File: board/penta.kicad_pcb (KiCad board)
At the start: 2 copper layers, 37.4 x 37.4 mm, 130 parts

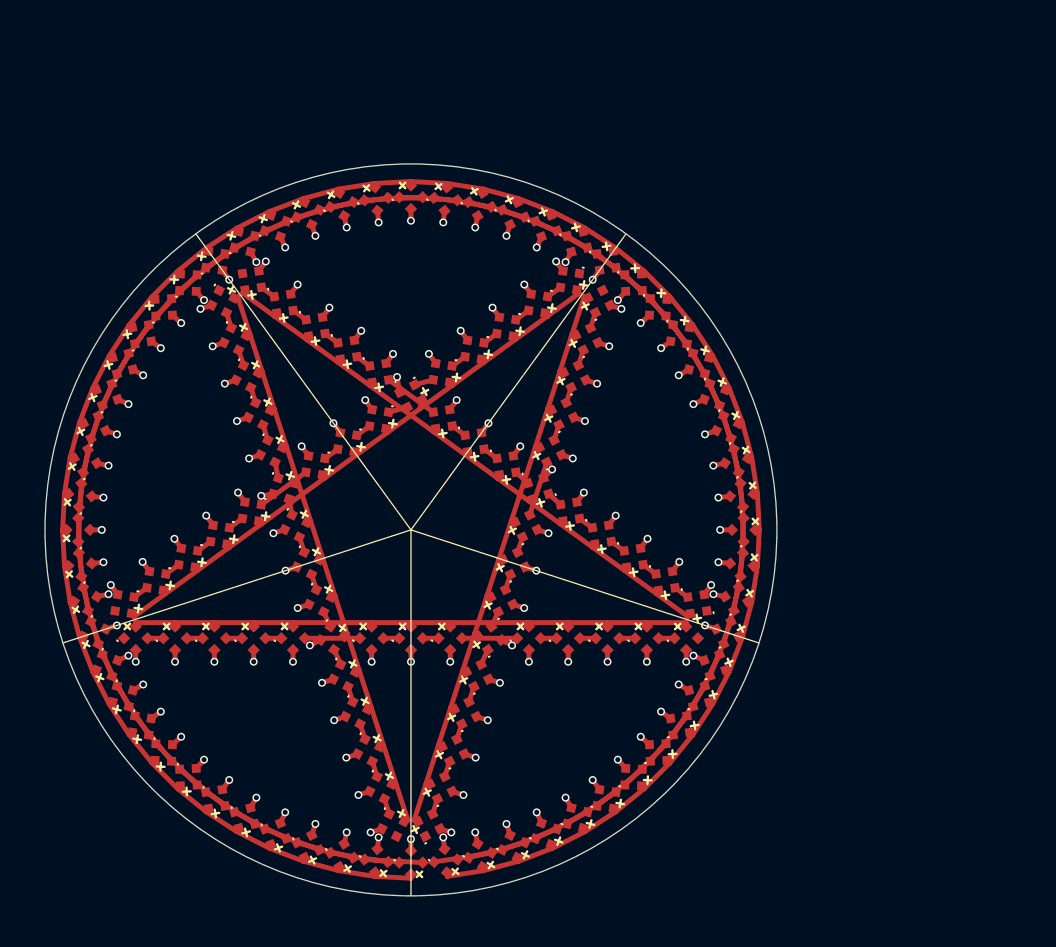
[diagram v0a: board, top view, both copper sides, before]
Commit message: candidate pixel layout + RP2040 + microphone + USB
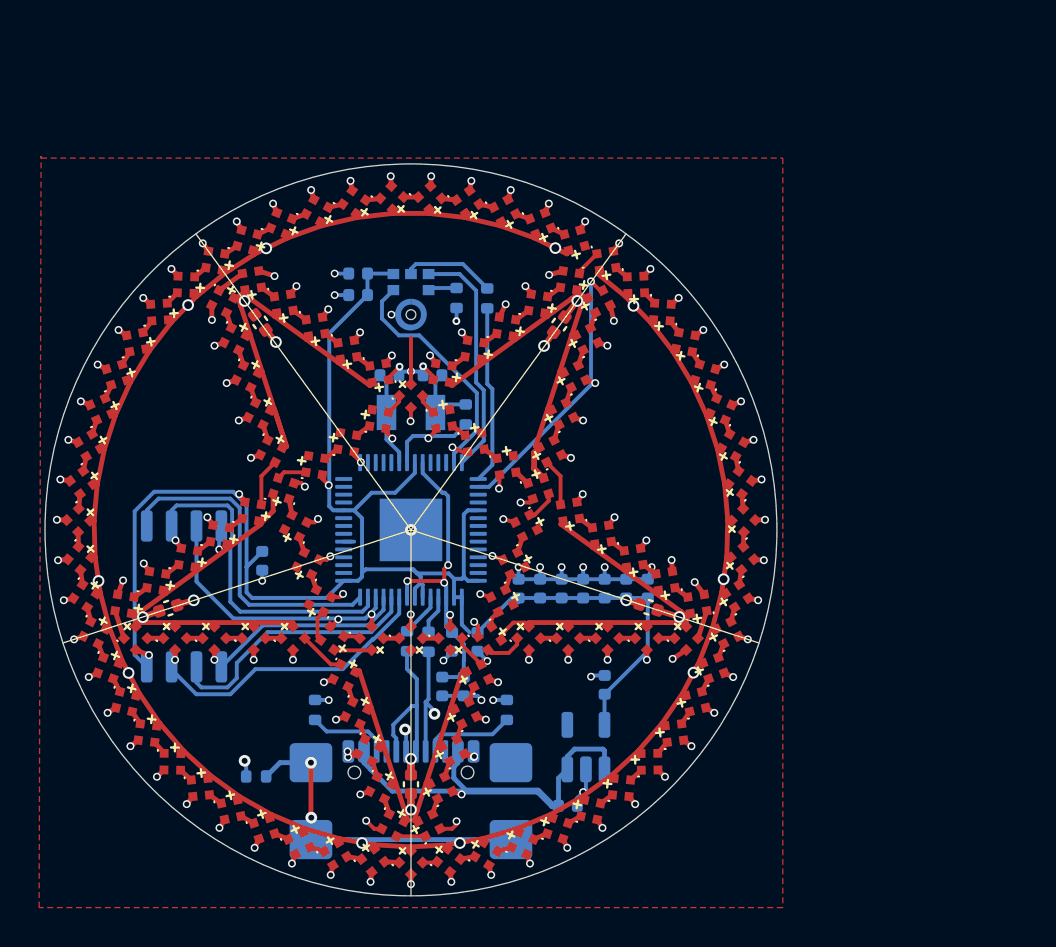
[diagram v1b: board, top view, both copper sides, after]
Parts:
- removed D126, D127, D128, D129, D130: XL-1010RGBC-WS2812B, ws2812b_1010
- added C10: 100n, Capacitor_SMD:C_0402_1005Metric, B.Cu at (106.6, 103.0)
- added C11: 100n, Capacitor_SMD:C_0402_1005Metric, B.Cu at (107.7, 103.0)
- added C12: 100n, Capacitor_SMD:C_0402_1005Metric, B.Cu at (108.8, 103.0)
- added C13: 100n, Capacitor_SMD:C_0402_1005Metric, B.Cu at (109.9, 103.0)
- added C14: 100n, Capacitor_SMD:C_0402_1005Metric, B.Cu at (111.0, 103.0)
- added C15: 100n, Capacitor_SMD:C_0402_1005Metric, B.Cu at (112.1, 103.0)
- added C16: 1u, Capacitor_SMD:C_0402_1005Metric, B.Cu at (102.1, 105.7)
- added C17: 100n, Capacitor_SMD:C_0402_1005Metric, B.Cu at (102.7, 108.0)
- added C18: 100n, Capacitor_SMD:C_0402_1005Metric, B.Cu at (101.6, 108.0)
- added C19: 100n, Capacitor_SMD:C_0402_1005Metric, B.Cu at (92.4, 101.6)
- added C2: 1uF, Capacitor_SMD:C_0402_1005Metric, B.Cu at (108.0, 114.1)
- added C20: 10u, Capacitor_SMD:C_0402_1005Metric, F.Cu at (100.0, 113.0)
- added C21: 10u, Capacitor_SMD:C_0402_1005Metric, F.Cu at (112.1, 104.0)
- added C22: 10u, Capacitor_SMD:C_0402_1005Metric, F.Cu at (107.6, 89.5)
- added C23: 10u, Capacitor_SMD:C_0402_1005Metric, F.Cu at (92.3, 89.4)
- added C24: 10u, Capacitor_SMD:C_0402_1005Metric, F.Cu at (87.6, 104.0)
- added C3: 1uF, Capacitor_SMD:C_0402_1005Metric, B.Cu at (109.9, 107.9)
- added C4: 220pF, Capacitor_SMD:C_0402_1005Metric, B.Cu at (97.3, 86.9)
- added C5: 1uF, Capacitor_SMD:C_0402_1005Metric, B.Cu at (97.3, 88.0)
- added C6: 27pF, Capacitor_SMD:C_0402_1005Metric, B.Cu at (98.9, 92.1)
- added C7: 27pF, Capacitor_SMD:C_0402_1005Metric, B.Cu at (101.1, 92.1)
- added C8: 1u, Capacitor_SMD:C_0402_1005Metric, B.Cu at (103.4, 105.7)
- added C9: 100n, Capacitor_SMD:C_0402_1005Metric, B.Cu at (105.5, 103.0)
- added J1: USB_C_Receptacle, Connector_USB:USB_C_Receptacle_GCT_USB4110, B.Cu at (100.0, 115.0)
- added MK1: SPH0645LM4H-B, penta:MIC_SPH0645LM4H-B, B.Cu at (100.0, 89.0)
- added R1: 5.11K, Resistor_SMD:R_0402_1005Metric, B.Cu at (104.9, 109.2)
- added R2: 5.11K, Resistor_SMD:R_0402_1005Metric, B.Cu at (95.1, 109.2)
- added R3: 1M, Resistor_SMD:R_0402_1005Metric, B.Cu at (92.1, 112.6)
- added R4: 68, Resistor_SMD:R_0402_1005Metric, B.Cu at (103.9, 88.2)
- added R5: 10K, Resistor_SMD:R_0402_1005Metric, B.Cu at (102.3, 88.2)
- added R6: 1k, Resistor_SMD:R_0402_1005Metric, B.Cu at (102.8, 94.1)
- added R7: 27, Resistor_SMD:R_0402_1005Metric, B.Cu at (100.9, 105.7)
- added R8: 27, Resistor_SMD:R_0402_1005Metric, B.Cu at (99.8, 105.7)
- added U1: MIC5504-3.3YM5, Package_TO_SOT_SMD:SOT-23-5, B.Cu at (108.9, 111.1)
- added U2: RP2040, Package_DFN_QFN:QFN-56-1EP_7x7mm_P0.4mm_EP3.2x3.2mm, B.Cu at (100.0, 100.0)
- added U3: W25Q32JVSS, Package_SO:SOIC-8_5.23x5.23mm_P1.27mm, B.Cu at (88.4, 103.4)
- added Y1: 12000Hz, Crystal:Crystal_SMD_3215-2Pin_3.2x1.5mm, B.Cu at (100.0, 94.0)
- D1, D10, D100, D101, D102, D103, D104, D105, D106, D107, D108, D109, D11, D110, D111, D112, D113, D114, D115, D116, D117, D118, D119, D12, D120, D121, D122, D123, D124, D125, D13, D14, D15, D16, D17, D18, D19, D2, D20, D21, D22, D23, D24, D25, D26, D27, D28, D29, D3, D30, D31, D32, D33, D34, D35, D36, D37, D38, D39, D4, D40, D41, D42, D43, D44, D45, D46, D47, D48, D49, D5, D50, D51, D52, D53, D54, D55, D56, D57, D58, D59, D6, D60, D61, D62, D63, D64, D65, D66, D67, D68, D69, D7, D70, D71, D72, D73, D74, D75, D76, D77, D78, D79, D8, D80, D81, D82, D83, D84, D85, D86, D87, D88, D89, D9, D90, D91, D92, D93, D94, D95, D96, D97, D98, D99: value XL-1010RGBC-WS2812B -> WS2812B; footprint ws2812b_1010 -> penta:ws2812b_1010
- moved D76 32.1 mm to (115.8, 93.8), turned to 156.273 degrees
- moved D90 31.9 mm to (105.7, 116.0), turned to 64.6364 degrees
- moved D117 31.7 mm to (93.4, 84.3), turned to -112.091 degrees
- moved D104 30.8 mm to (83.8, 105.3), turned to -27 degrees
- moved D60 30.8 mm to (90.4, 88.3), turned to -27 degrees
- moved D103 30.3 mm to (84.5, 107.1), turned to -20.4545 degrees
- moved D77 30.3 mm to (116.4, 95.7), turned to 149.727 degrees
- moved D1 30.2 mm to (109.6, 88.3), turned to 117 degrees
- moved D91 30.0 mm to (103.9, 116.6), turned to 58.0909 degrees
- moved D51 29.7 mm to (85.4, 103.8), turned to -99 degrees
- moved D116 29.7 mm to (91.6, 85.2), turned to -105.545 degrees
- moved D50 29.6 mm to (85.9, 105.5), turned to 45 degrees
- moved D59 29.2 mm to (91.0, 90.2), turned to -27 degrees
- moved D10 29.1 mm to (114.6, 103.8), turned to -171 degrees
- moved D11 28.9 mm to (114.1, 105.5), turned to 45 degrees
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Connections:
- D1 pad 1: (no net) -> Net-(D1-DOUT)
- D1 pad 2: (no net) -> +5V
- D1 pad 3: (no net) -> GND
- D1 pad 4: (no net) -> /LED_DATA
- D10 pad 1: (no net) -> Net-(D10-DOUT)
- D10 pad 2: (no net) -> +5V
- D10 pad 3: (no net) -> GND
- D10 pad 4: (no net) -> Net-(D10-DIN)
- D100 pad 1: (no net) -> Net-(D100-DOUT)
- D100 pad 2: (no net) -> +5V
- D100 pad 3: (no net) -> GND
- D100 pad 4: (no net) -> Net-(D100-DIN)
- D101 pad 1: (no net) -> Net-(D101-DOUT)
- D101 pad 2: (no net) -> +5V
- D101 pad 3: (no net) -> GND
- D101 pad 4: (no net) -> Net-(D100-DOUT)
- D102 pad 1: (no net) -> Net-(D102-DOUT)
- D102 pad 2: (no net) -> +5V
- D102 pad 3: (no net) -> GND
- D102 pad 4: (no net) -> Net-(D101-DOUT)
- D103 pad 1: (no net) -> Net-(D103-DOUT)
- D103 pad 2: (no net) -> +5V
- D103 pad 3: (no net) -> GND
- D103 pad 4: (no net) -> Net-(D102-DOUT)
- D104 pad 1: (no net) -> Net-(D104-DOUT)
- D104 pad 2: (no net) -> +5V
- D104 pad 3: (no net) -> GND
- D104 pad 4: (no net) -> Net-(D103-DOUT)
- D105 pad 1: (no net) -> Net-(D105-DOUT)
- D105 pad 2: (no net) -> +5V
- D105 pad 3: (no net) -> GND
- D105 pad 4: (no net) -> Net-(D104-DOUT)
- D106 pad 1: (no net) -> Net-(D106-DOUT)
- D106 pad 2: (no net) -> +5V
- D106 pad 3: (no net) -> GND
- D106 pad 4: (no net) -> Net-(D105-DOUT)
- D107 pad 1: (no net) -> Net-(D107-DOUT)
- D107 pad 2: (no net) -> +5V
- D107 pad 3: (no net) -> GND
- D107 pad 4: (no net) -> Net-(D106-DOUT)
- D108 pad 1: (no net) -> Net-(D108-DOUT)
- D108 pad 2: (no net) -> +5V
- D108 pad 3: (no net) -> GND
- D108 pad 4: (no net) -> Net-(D107-DOUT)
- D109 pad 1: (no net) -> Net-(D109-DOUT)
- D109 pad 2: (no net) -> +5V
- D109 pad 3: (no net) -> GND
- D109 pad 4: (no net) -> Net-(D108-DOUT)
- D11 pad 1: (no net) -> Net-(D11-DOUT)
- D11 pad 2: (no net) -> +5V
- D11 pad 3: (no net) -> GND
- D11 pad 4: (no net) -> Net-(D10-DOUT)
- D110 pad 1: (no net) -> Net-(D110-DOUT)
- D110 pad 2: (no net) -> +5V
- D110 pad 3: (no net) -> GND
- D110 pad 4: (no net) -> Net-(D109-DOUT)
- D111 pad 1: (no net) -> Net-(D111-DOUT)
- D111 pad 2: (no net) -> +5V
- D111 pad 3: (no net) -> GND
- D111 pad 4: (no net) -> Net-(D110-DOUT)
- D112 pad 1: (no net) -> Net-(D112-DOUT)
- D112 pad 2: (no net) -> +5V
- D112 pad 3: (no net) -> GND
- D112 pad 4: (no net) -> Net-(D111-DOUT)
- D113 pad 1: (no net) -> Net-(D113-DOUT)
- D113 pad 2: (no net) -> +5V
- D113 pad 3: (no net) -> GND
- D113 pad 4: (no net) -> Net-(D112-DOUT)
- D114 pad 1: (no net) -> Net-(D114-DOUT)
- D114 pad 2: (no net) -> +5V
- D114 pad 3: (no net) -> GND
- D114 pad 4: (no net) -> Net-(D113-DOUT)
- D115 pad 1: (no net) -> Net-(D115-DOUT)
- D115 pad 2: (no net) -> +5V
- D115 pad 3: (no net) -> GND
- D115 pad 4: (no net) -> Net-(D114-DOUT)
- D116 pad 1: (no net) -> Net-(D116-DOUT)
- D116 pad 2: (no net) -> +5V
- D116 pad 3: (no net) -> GND
- D116 pad 4: (no net) -> Net-(D115-DOUT)
- D117 pad 1: (no net) -> Net-(D117-DOUT)
- D117 pad 2: (no net) -> +5V
- D117 pad 3: (no net) -> GND
- D117 pad 4: (no net) -> Net-(D116-DOUT)
- D118 pad 1: (no net) -> Net-(D118-DOUT)
- D118 pad 2: (no net) -> +5V
- D118 pad 3: (no net) -> GND
- D118 pad 4: (no net) -> Net-(D117-DOUT)
- D119 pad 1: (no net) -> Net-(D119-DOUT)
- D119 pad 2: (no net) -> +5V
- D119 pad 3: (no net) -> GND
- D119 pad 4: (no net) -> Net-(D118-DOUT)
- D12 pad 1: (no net) -> Net-(D12-DOUT)
- D12 pad 2: (no net) -> +5V
- D12 pad 3: (no net) -> GND
- D12 pad 4: (no net) -> Net-(D11-DOUT)
- D120 pad 1: (no net) -> Net-(D120-DOUT)
- D120 pad 2: (no net) -> +5V
- D120 pad 3: (no net) -> GND
- D120 pad 4: (no net) -> Net-(D119-DOUT)
- D121 pad 1: (no net) -> Net-(D121-DOUT)
- D121 pad 2: (no net) -> +5V
- D121 pad 3: (no net) -> GND
- D121 pad 4: (no net) -> Net-(D120-DOUT)
- D122 pad 1: (no net) -> Net-(D122-DOUT)
- D122 pad 2: (no net) -> +5V
- D122 pad 3: (no net) -> GND
- D122 pad 4: (no net) -> Net-(D121-DOUT)
- D123 pad 1: (no net) -> Net-(D123-DOUT)
- D123 pad 2: (no net) -> +5V
- D123 pad 3: (no net) -> GND
- D123 pad 4: (no net) -> Net-(D122-DOUT)
- D124 pad 1: (no net) -> Net-(D124-DOUT)
- D124 pad 2: (no net) -> +5V
- D124 pad 3: (no net) -> GND
- D124 pad 4: (no net) -> Net-(D123-DOUT)
- D125 pad 1: (no net) -> unconnected-(D125-DOUT-Pad1)
- D125 pad 2: (no net) -> +5V
- D125 pad 3: (no net) -> GND
- D125 pad 4: (no net) -> Net-(D124-DOUT)
- D13 pad 1: (no net) -> Net-(D13-DOUT)
- D13 pad 2: (no net) -> +5V
- D13 pad 3: (no net) -> GND
- D13 pad 4: (no net) -> Net-(D12-DOUT)
- D14 pad 1: (no net) -> Net-(D14-DOUT)
- D14 pad 2: (no net) -> +5V
- D14 pad 3: (no net) -> GND
- D14 pad 4: (no net) -> Net-(D13-DOUT)
- D15 pad 1: (no net) -> Net-(D15-DOUT)
- D15 pad 2: (no net) -> +5V
- D15 pad 3: (no net) -> GND
- D15 pad 4: (no net) -> Net-(D14-DOUT)
- D16 pad 1: (no net) -> Net-(D16-DOUT)
- D16 pad 2: (no net) -> +5V
- D16 pad 3: (no net) -> GND
- D16 pad 4: (no net) -> Net-(D15-DOUT)
- D17 pad 1: (no net) -> Net-(D17-DOUT)
- D17 pad 2: (no net) -> +5V
- D17 pad 3: (no net) -> GND
- D17 pad 4: (no net) -> Net-(D16-DOUT)
- D18 pad 1: (no net) -> Net-(D18-DOUT)
- D18 pad 2: (no net) -> +5V
- D18 pad 3: (no net) -> GND
- D18 pad 4: (no net) -> Net-(D17-DOUT)
- D19 pad 1: (no net) -> Net-(D19-DOUT)
- D19 pad 2: (no net) -> +5V
- D19 pad 3: (no net) -> GND
- D19 pad 4: (no net) -> Net-(D18-DOUT)
- D2 pad 1: (no net) -> Net-(D2-DOUT)
- D2 pad 2: (no net) -> +5V
- D2 pad 3: (no net) -> GND
- D2 pad 4: (no net) -> Net-(D1-DOUT)
- D20 pad 1: (no net) -> Net-(D20-DOUT)
- D20 pad 2: (no net) -> +5V
- D20 pad 3: (no net) -> GND
- D20 pad 4: (no net) -> Net-(D19-DOUT)
- D21 pad 1: (no net) -> Net-(D21-DOUT)
- D21 pad 2: (no net) -> +5V
- D21 pad 3: (no net) -> GND
- D21 pad 4: (no net) -> Net-(D20-DOUT)
- D22 pad 1: (no net) -> Net-(D22-DOUT)
- D22 pad 2: (no net) -> +5V
- D22 pad 3: (no net) -> GND
- D22 pad 4: (no net) -> Net-(D21-DOUT)
- D23 pad 1: (no net) -> Net-(D23-DOUT)
- D23 pad 2: (no net) -> +5V
- D23 pad 3: (no net) -> GND
- D23 pad 4: (no net) -> Net-(D22-DOUT)
- D24 pad 1: (no net) -> Net-(D24-DOUT)
- D24 pad 2: (no net) -> +5V
- D24 pad 3: (no net) -> GND
- D24 pad 4: (no net) -> Net-(D23-DOUT)
- D25 pad 1: (no net) -> Net-(D25-DOUT)
- D25 pad 2: (no net) -> +5V
- D25 pad 3: (no net) -> GND
- D25 pad 4: (no net) -> Net-(D24-DOUT)
- D26 pad 1: (no net) -> Net-(D26-DOUT)
- D26 pad 2: (no net) -> +5V
- D26 pad 3: (no net) -> GND
- D26 pad 4: (no net) -> Net-(D25-DOUT)
- D27 pad 1: (no net) -> Net-(D27-DOUT)
- D27 pad 2: (no net) -> +5V
- D27 pad 3: (no net) -> GND
- D27 pad 4: (no net) -> Net-(D26-DOUT)
- D28 pad 1: (no net) -> Net-(D28-DOUT)
- D28 pad 2: (no net) -> +5V
- D28 pad 3: (no net) -> GND
- D28 pad 4: (no net) -> Net-(D27-DOUT)
- D29 pad 1: (no net) -> Net-(D29-DOUT)
- D29 pad 2: (no net) -> +5V
- D29 pad 3: (no net) -> GND
- D29 pad 4: (no net) -> Net-(D28-DOUT)
- D3 pad 1: (no net) -> Net-(D3-DOUT)
- D3 pad 2: (no net) -> +5V
- D3 pad 3: (no net) -> GND
- D3 pad 4: (no net) -> Net-(D2-DOUT)
- D30 pad 1: (no net) -> Net-(D30-DOUT)
- D30 pad 2: (no net) -> +5V
- D30 pad 3: (no net) -> GND
- D30 pad 4: (no net) -> Net-(D29-DOUT)
- D31 pad 1: (no net) -> Net-(D31-DOUT)
- D31 pad 2: (no net) -> +5V
- D31 pad 3: (no net) -> GND
- D31 pad 4: (no net) -> Net-(D30-DOUT)
- D32 pad 1: (no net) -> Net-(D32-DOUT)
- D32 pad 2: (no net) -> +5V
- D32 pad 3: (no net) -> GND
- D32 pad 4: (no net) -> Net-(D31-DOUT)
- D33 pad 1: (no net) -> Net-(D33-DOUT)
- D33 pad 2: (no net) -> +5V
- D33 pad 3: (no net) -> GND
- D33 pad 4: (no net) -> Net-(D32-DOUT)
- D34 pad 1: (no net) -> Net-(D34-DOUT)
- D34 pad 2: (no net) -> +5V
- D34 pad 3: (no net) -> GND
- D34 pad 4: (no net) -> Net-(D33-DOUT)
- D35 pad 1: (no net) -> Net-(D35-DOUT)
- D35 pad 2: (no net) -> +5V
- D35 pad 3: (no net) -> GND
- D35 pad 4: (no net) -> Net-(D34-DOUT)
- D36 pad 1: (no net) -> Net-(D36-DOUT)
- D36 pad 2: (no net) -> +5V
- D36 pad 3: (no net) -> GND
- D36 pad 4: (no net) -> Net-(D35-DOUT)
- D37 pad 1: (no net) -> Net-(D37-DOUT)
- D37 pad 2: (no net) -> +5V
- D37 pad 3: (no net) -> GND
- D37 pad 4: (no net) -> Net-(D36-DOUT)
- D38 pad 1: (no net) -> Net-(D38-DOUT)
- D38 pad 2: (no net) -> +5V
- D38 pad 3: (no net) -> GND
- D38 pad 4: (no net) -> Net-(D37-DOUT)
- D39 pad 1: (no net) -> Net-(D39-DOUT)
- D39 pad 2: (no net) -> +5V
- D39 pad 3: (no net) -> GND
- D39 pad 4: (no net) -> Net-(D38-DOUT)
- D4 pad 1: (no net) -> Net-(D4-DOUT)
- D4 pad 2: (no net) -> +5V
- D4 pad 3: (no net) -> GND
- D4 pad 4: (no net) -> Net-(D3-DOUT)
- D40 pad 1: (no net) -> Net-(D40-DOUT)
- D40 pad 2: (no net) -> +5V
- D40 pad 3: (no net) -> GND
- D40 pad 4: (no net) -> Net-(D39-DOUT)
- D41 pad 1: (no net) -> Net-(D41-DOUT)
- D41 pad 2: (no net) -> +5V
- D41 pad 3: (no net) -> GND
- D41 pad 4: (no net) -> Net-(D40-DOUT)
- D42 pad 1: (no net) -> Net-(D42-DOUT)
- D42 pad 2: (no net) -> +5V
- D42 pad 3: (no net) -> GND
- D42 pad 4: (no net) -> Net-(D41-DOUT)
- D43 pad 1: (no net) -> Net-(D43-DOUT)
- D43 pad 2: (no net) -> +5V
- D43 pad 3: (no net) -> GND
- D43 pad 4: (no net) -> Net-(D42-DOUT)
- D44 pad 1: (no net) -> Net-(D44-DOUT)
- D44 pad 2: (no net) -> +5V
- D44 pad 3: (no net) -> GND
- D44 pad 4: (no net) -> Net-(D43-DOUT)
- D45 pad 1: (no net) -> Net-(D45-DOUT)
- D45 pad 2: (no net) -> +5V
- D45 pad 3: (no net) -> GND
- D45 pad 4: (no net) -> Net-(D44-DOUT)
- D46 pad 1: (no net) -> Net-(D46-DOUT)
- D46 pad 2: (no net) -> +5V
- D46 pad 3: (no net) -> GND
- D46 pad 4: (no net) -> Net-(D45-DOUT)
- D47 pad 1: (no net) -> Net-(D47-DOUT)
- D47 pad 2: (no net) -> +5V
- D47 pad 3: (no net) -> GND
- D47 pad 4: (no net) -> Net-(D46-DOUT)
- D48 pad 1: (no net) -> Net-(D48-DOUT)
- D48 pad 2: (no net) -> +5V
- D48 pad 3: (no net) -> GND
- D48 pad 4: (no net) -> Net-(D47-DOUT)
- D49 pad 1: (no net) -> Net-(D49-DOUT)
- D49 pad 2: (no net) -> +5V
- D49 pad 3: (no net) -> GND
- D49 pad 4: (no net) -> Net-(D48-DOUT)
- D5 pad 1: (no net) -> Net-(D5-DOUT)
- D5 pad 2: (no net) -> +5V
- D5 pad 3: (no net) -> GND
- D5 pad 4: (no net) -> Net-(D4-DOUT)
- D50 pad 1: (no net) -> Net-(D50-DOUT)
- D50 pad 2: (no net) -> +5V
- D50 pad 3: (no net) -> GND
- D50 pad 4: (no net) -> Net-(D49-DOUT)
- D51 pad 1: (no net) -> Net-(D51-DOUT)
- D51 pad 2: (no net) -> +5V
- D51 pad 3: (no net) -> GND
- D51 pad 4: (no net) -> Net-(D50-DOUT)
- D52 pad 1: (no net) -> Net-(D52-DOUT)
- D52 pad 2: (no net) -> +5V
- D52 pad 3: (no net) -> GND
- D52 pad 4: (no net) -> Net-(D51-DOUT)
- D53 pad 1: (no net) -> Net-(D53-DOUT)
- D53 pad 2: (no net) -> +5V
- D53 pad 3: (no net) -> GND
- D53 pad 4: (no net) -> Net-(D52-DOUT)
- D54 pad 1: (no net) -> Net-(D54-DOUT)
- D54 pad 2: (no net) -> +5V
- D54 pad 3: (no net) -> GND
- D54 pad 4: (no net) -> Net-(D53-DOUT)
- D55 pad 1: (no net) -> Net-(D55-DOUT)
- D55 pad 2: (no net) -> +5V
- D55 pad 3: (no net) -> GND
- D55 pad 4: (no net) -> Net-(D54-DOUT)
- D56 pad 1: (no net) -> Net-(D56-DOUT)
- D56 pad 2: (no net) -> +5V
- D56 pad 3: (no net) -> GND
- D56 pad 4: (no net) -> Net-(D55-DOUT)
- D57 pad 1: (no net) -> Net-(D57-DOUT)
- D57 pad 2: (no net) -> +5V
- D57 pad 3: (no net) -> GND
- D57 pad 4: (no net) -> Net-(D56-DOUT)
- D58 pad 1: (no net) -> Net-(D58-DOUT)
- D58 pad 2: (no net) -> +5V
- D58 pad 3: (no net) -> GND
- D58 pad 4: (no net) -> Net-(D57-DOUT)
- D59 pad 1: (no net) -> Net-(D59-DOUT)
- D59 pad 2: (no net) -> +5V
- D59 pad 3: (no net) -> GND
- D59 pad 4: (no net) -> Net-(D58-DOUT)
- D6 pad 1: (no net) -> Net-(D6-DOUT)
- D6 pad 2: (no net) -> +5V
- D6 pad 3: (no net) -> GND
- D6 pad 4: (no net) -> Net-(D5-DOUT)
- D60 pad 1: (no net) -> Net-(D60-DOUT)
- D60 pad 2: (no net) -> +5V
- D60 pad 3: (no net) -> GND
- D60 pad 4: (no net) -> Net-(D59-DOUT)
- D61 pad 1: (no net) -> Net-(D61-DOUT)
- D61 pad 2: (no net) -> +5V
- D61 pad 3: (no net) -> GND
- D61 pad 4: (no net) -> Net-(D60-DOUT)
- D62 pad 1: (no net) -> Net-(D62-DOUT)
- D62 pad 2: (no net) -> +5V
- D62 pad 3: (no net) -> GND
- D62 pad 4: (no net) -> Net-(D61-DOUT)
- D63 pad 1: (no net) -> Net-(D63-DOUT)
- D63 pad 2: (no net) -> +5V
- D63 pad 3: (no net) -> GND
- D63 pad 4: (no net) -> Net-(D62-DOUT)
- D64 pad 1: (no net) -> Net-(D64-DOUT)
- D64 pad 2: (no net) -> +5V
- D64 pad 3: (no net) -> GND
- D64 pad 4: (no net) -> Net-(D63-DOUT)
- D65 pad 1: (no net) -> Net-(D65-DOUT)
- D65 pad 2: (no net) -> +5V
- D65 pad 3: (no net) -> GND
- D65 pad 4: (no net) -> Net-(D64-DOUT)
- D66 pad 1: (no net) -> Net-(D66-DOUT)
- D66 pad 2: (no net) -> +5V
- D66 pad 3: (no net) -> GND
- D66 pad 4: (no net) -> Net-(D65-DOUT)
- D67 pad 1: (no net) -> Net-(D67-DOUT)
- D67 pad 2: (no net) -> +5V
- D67 pad 3: (no net) -> GND
- D67 pad 4: (no net) -> Net-(D66-DOUT)
- D68 pad 1: (no net) -> Net-(D68-DOUT)
- D68 pad 2: (no net) -> +5V
- D68 pad 3: (no net) -> GND
- D68 pad 4: (no net) -> Net-(D67-DOUT)
- D69 pad 1: (no net) -> Net-(D69-DOUT)
- D69 pad 2: (no net) -> +5V
- D69 pad 3: (no net) -> GND
- D69 pad 4: (no net) -> Net-(D68-DOUT)
- D7 pad 1: (no net) -> Net-(D7-DOUT)
- D7 pad 2: (no net) -> +5V
- D7 pad 3: (no net) -> GND
- D7 pad 4: (no net) -> Net-(D6-DOUT)
- D70 pad 1: (no net) -> Net-(D70-DOUT)
- D70 pad 2: (no net) -> +5V
- D70 pad 3: (no net) -> GND
- D70 pad 4: (no net) -> Net-(D69-DOUT)
- D71 pad 1: (no net) -> Net-(D71-DOUT)
- D71 pad 2: (no net) -> +5V
- D71 pad 3: (no net) -> GND
- D71 pad 4: (no net) -> Net-(D70-DOUT)
- D72 pad 1: (no net) -> Net-(D72-DOUT)
- D72 pad 2: (no net) -> +5V
- D72 pad 3: (no net) -> GND
- D72 pad 4: (no net) -> Net-(D71-DOUT)
- D73 pad 1: (no net) -> Net-(D73-DOUT)
- D73 pad 2: (no net) -> +5V
- D73 pad 3: (no net) -> GND
- D73 pad 4: (no net) -> Net-(D72-DOUT)
- D74 pad 1: (no net) -> Net-(D74-DOUT)
- D74 pad 2: (no net) -> +5V
- D74 pad 3: (no net) -> GND
- D74 pad 4: (no net) -> Net-(D73-DOUT)
- D75 pad 1: (no net) -> Net-(D75-DOUT)
- D75 pad 2: (no net) -> +5V
- D75 pad 3: (no net) -> GND
- D75 pad 4: (no net) -> Net-(D74-DOUT)
- D76 pad 1: (no net) -> Net-(D76-DOUT)
- D76 pad 2: (no net) -> +5V
- D76 pad 3: (no net) -> GND
- D76 pad 4: (no net) -> Net-(D75-DOUT)
- D77 pad 1: (no net) -> Net-(D77-DOUT)
- D77 pad 2: (no net) -> +5V
- D77 pad 3: (no net) -> GND
- D77 pad 4: (no net) -> Net-(D76-DOUT)
- D78 pad 1: (no net) -> Net-(D78-DOUT)
- D78 pad 2: (no net) -> +5V
- D78 pad 3: (no net) -> GND
- D78 pad 4: (no net) -> Net-(D77-DOUT)
- D79 pad 1: (no net) -> Net-(D79-DOUT)
- D79 pad 2: (no net) -> +5V
- D79 pad 3: (no net) -> GND
- D79 pad 4: (no net) -> Net-(D78-DOUT)
- D8 pad 1: (no net) -> Net-(D8-DOUT)
- D8 pad 2: (no net) -> +5V
- D8 pad 3: (no net) -> GND
- D8 pad 4: (no net) -> Net-(D7-DOUT)
- D80 pad 1: (no net) -> Net-(D80-DOUT)
- D80 pad 2: (no net) -> +5V
- D80 pad 3: (no net) -> GND
- D80 pad 4: (no net) -> Net-(D79-DOUT)
- D81 pad 1: (no net) -> Net-(D81-DOUT)
- D81 pad 2: (no net) -> +5V
- D81 pad 3: (no net) -> GND
- D81 pad 4: (no net) -> Net-(D80-DOUT)
- D82 pad 1: (no net) -> Net-(D82-DOUT)
- D82 pad 2: (no net) -> +5V
- D82 pad 3: (no net) -> GND
- D82 pad 4: (no net) -> Net-(D81-DOUT)
- D83 pad 1: (no net) -> Net-(D83-DOUT)
- D83 pad 2: (no net) -> +5V
- D83 pad 3: (no net) -> GND
- D83 pad 4: (no net) -> Net-(D82-DOUT)
- D84 pad 1: (no net) -> Net-(D84-DOUT)
- D84 pad 2: (no net) -> +5V
- D84 pad 3: (no net) -> GND
- D84 pad 4: (no net) -> Net-(D83-DOUT)
- D85 pad 1: (no net) -> Net-(D85-DOUT)
- D85 pad 2: (no net) -> +5V
- D85 pad 3: (no net) -> GND
- D85 pad 4: (no net) -> Net-(D84-DOUT)
- D86 pad 1: (no net) -> Net-(D86-DOUT)
- D86 pad 2: (no net) -> +5V
- D86 pad 3: (no net) -> GND
- D86 pad 4: (no net) -> Net-(D85-DOUT)
- D87 pad 1: (no net) -> Net-(D87-DOUT)
- D87 pad 2: (no net) -> +5V
- D87 pad 3: (no net) -> GND
- D87 pad 4: (no net) -> Net-(D86-DOUT)
- D88 pad 1: (no net) -> Net-(D88-DOUT)
- D88 pad 2: (no net) -> +5V
- D88 pad 3: (no net) -> GND
- D88 pad 4: (no net) -> Net-(D87-DOUT)
- D89 pad 1: (no net) -> Net-(D89-DOUT)
- D89 pad 2: (no net) -> +5V
- D89 pad 3: (no net) -> GND
- D89 pad 4: (no net) -> Net-(D88-DOUT)
- D9 pad 1: (no net) -> Net-(D10-DIN)
- D9 pad 2: (no net) -> +5V
- D9 pad 3: (no net) -> GND
- D9 pad 4: (no net) -> Net-(D8-DOUT)
- D90 pad 1: (no net) -> Net-(D90-DOUT)
- D90 pad 2: (no net) -> +5V
- D90 pad 3: (no net) -> GND
- D90 pad 4: (no net) -> Net-(D89-DOUT)
- D91 pad 1: (no net) -> Net-(D91-DOUT)
- D91 pad 2: (no net) -> +5V
- D91 pad 3: (no net) -> GND
- D91 pad 4: (no net) -> Net-(D90-DOUT)
- D92 pad 1: (no net) -> Net-(D92-DOUT)
- D92 pad 2: (no net) -> +5V
- D92 pad 3: (no net) -> GND
- D92 pad 4: (no net) -> Net-(D91-DOUT)
- D93 pad 1: (no net) -> Net-(D93-DOUT)
- D93 pad 2: (no net) -> +5V
- D93 pad 3: (no net) -> GND
- D93 pad 4: (no net) -> Net-(D92-DOUT)
- D94 pad 1: (no net) -> Net-(D94-DOUT)
- D94 pad 2: (no net) -> +5V
- D94 pad 3: (no net) -> GND
- D94 pad 4: (no net) -> Net-(D93-DOUT)
- D95 pad 1: (no net) -> Net-(D95-DOUT)
- D95 pad 2: (no net) -> +5V
- D95 pad 3: (no net) -> GND
- D95 pad 4: (no net) -> Net-(D94-DOUT)
- D96 pad 1: (no net) -> Net-(D96-DOUT)
- D96 pad 2: (no net) -> +5V
- D96 pad 3: (no net) -> GND
- D96 pad 4: (no net) -> Net-(D95-DOUT)
- D97 pad 1: (no net) -> Net-(D97-DOUT)
- D97 pad 2: (no net) -> +5V
- D97 pad 3: (no net) -> GND
- D97 pad 4: (no net) -> Net-(D96-DOUT)
- D98 pad 1: (no net) -> Net-(D98-DOUT)
- D98 pad 2: (no net) -> +5V
- D98 pad 3: (no net) -> GND
- D98 pad 4: (no net) -> Net-(D97-DOUT)
- D99 pad 1: (no net) -> Net-(D100-DIN)
- D99 pad 2: (no net) -> +5V
- D99 pad 3: (no net) -> GND
- D99 pad 4: (no net) -> Net-(D98-DOUT)
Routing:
- net (no net): track 594.0 -> 0.00 mm, vias 130 -> 0
- net +5V: track 0.00 -> 270.7 mm, vias 0 -> 15
- net GND: track 0.00 -> 99.6 mm, vias 0 -> 155
- net +3V3: track 0.00 -> 83.3 mm
- net /QSPI_SS: track 0.00 -> 17.0 mm
- net Net-(J1-SHIELD): track 0.00 -> 16.7 mm, vias 0 -> 2
- net /QSPI1: track 0.00 -> 16.6 mm
- net +1V1: track 0.00 -> 16.0 mm, vias 0 -> 3
- net /QSPI3: track 0.00 -> 14.8 mm
- net /LED_DATA: track 0.00 -> 14.0 mm, vias 0 -> 1
- net /QSPI_SCK: track 0.00 -> 13.7 mm
- net /QSPI2: track 0.00 -> 13.6 mm
- net Net-(MK1-WS): track 0.00 -> 12.2 mm
- net Net-(MK1-BCLK): track 0.00 -> 12.2 mm
- net /QSPI0: track 0.00 -> 10.1 mm
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- added copper zone on F.Cu, net +5V
- added copper zone on In1.Cu, net GND
- added copper zone on In2.Cu, net GND
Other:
- copper layers 2 -> 4

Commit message: remove the 5v net
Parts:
- turned D24 to 90 degrees
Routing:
- net +5V: track 270.7 -> 302.3 mm
- net GND: track 99.6 -> 101.8 mm, vias 155 -> 153
- net Net-(D65-DOUT): track 3.01 -> 2.71 mm, vias 2 -> 0
- removed copper zone on F.Cu, net +5V

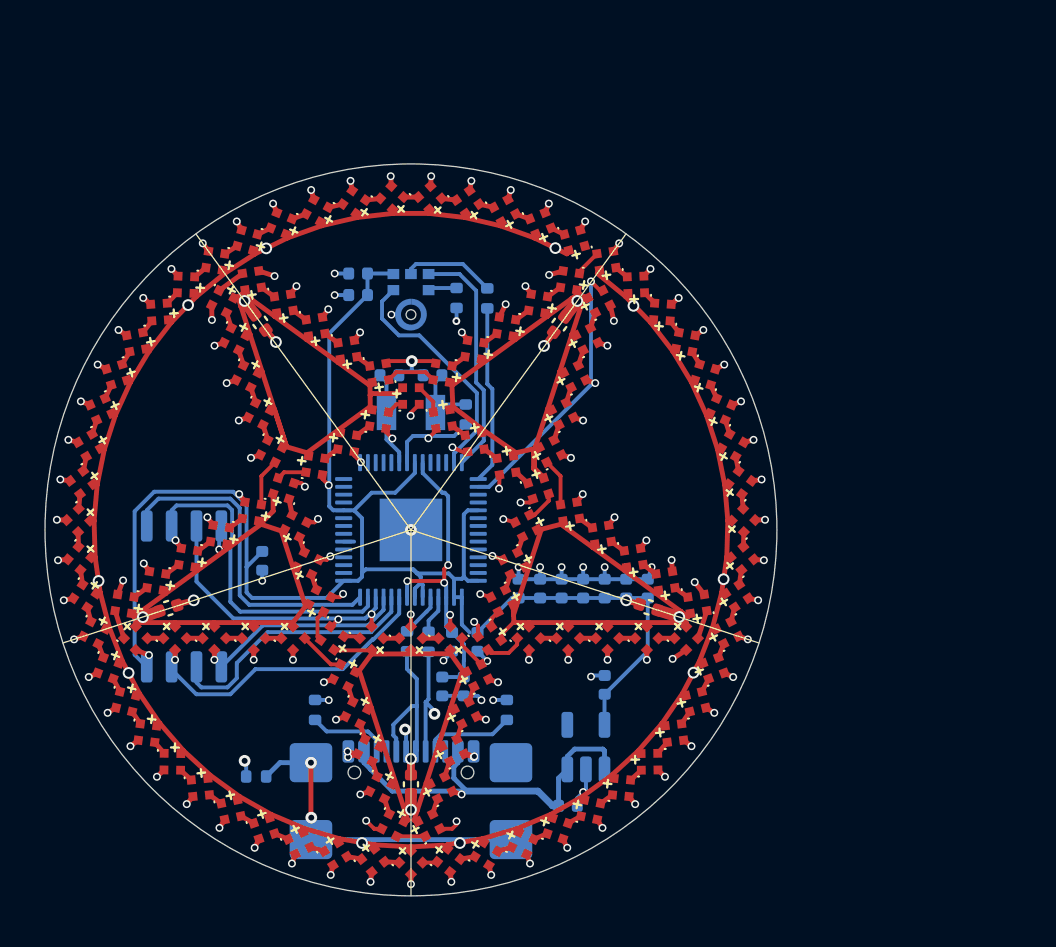
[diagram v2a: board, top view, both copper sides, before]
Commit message: schematic for a boost chip that we may not actually need; + wc changes
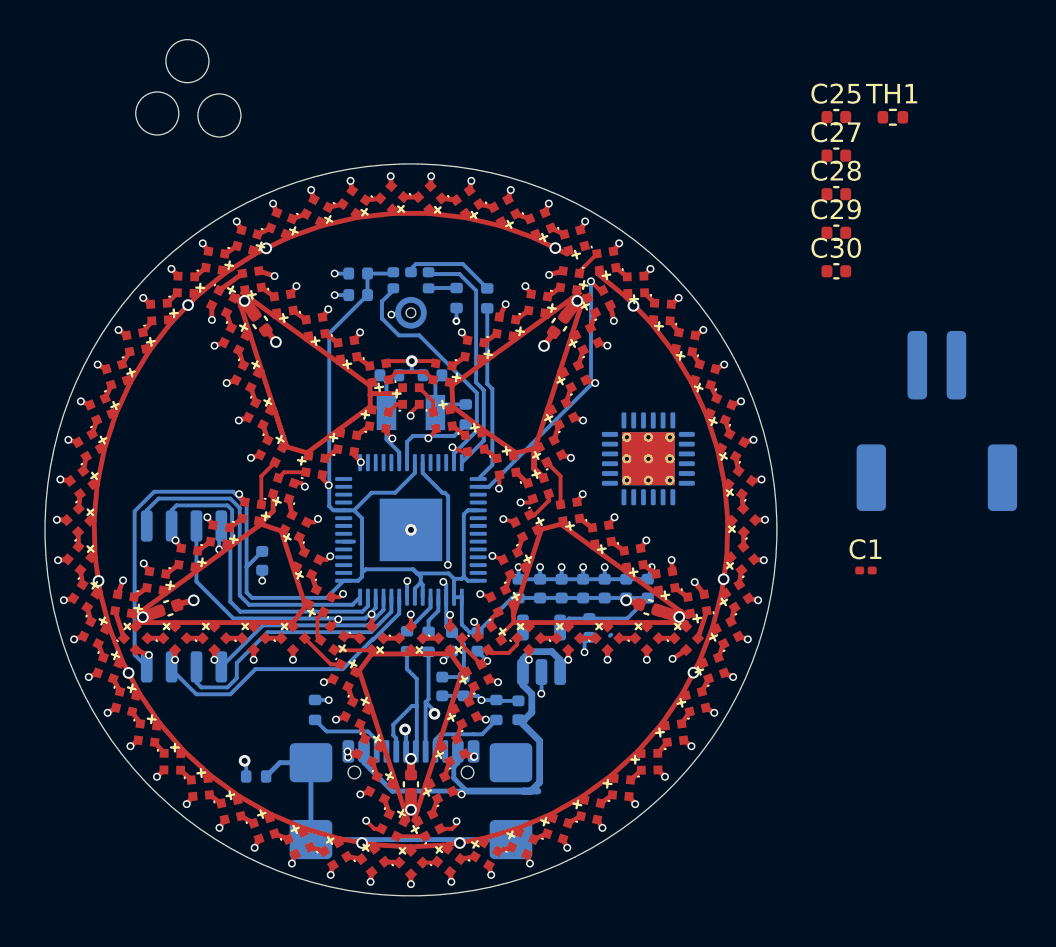
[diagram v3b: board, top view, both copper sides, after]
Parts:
- added C1: 40u, Capacitor_SMD:C_0201_0603Metric, F.Cu at (123.2, 102.1)
- added C25: 10uF, Capacitor_SMD:C_0402_1005Metric, F.Cu at (121.7, 78.9)
- added C27: 1u, Capacitor_SMD:C_0402_1005Metric, F.Cu at (121.7, 80.9)
- added C28: 47n, Capacitor_SMD:C_0402_1005Metric, F.Cu at (121.7, 82.8)
- added C29: 1u, Capacitor_SMD:C_0402_1005Metric, F.Cu at (121.7, 84.8)
- added C30: 1u, Capacitor_SMD:C_0402_1005Metric, F.Cu at (121.7, 86.8)
- added J2: Conn_01x02, Connector_JST:JST_PH_S2B-PH-SM4-TB_1x02-1MP_P2.00mm_Horizontal, B.Cu at (126.9, 94.4)
- added TH1: Thermistor_NTC, Resistor_SMD:R_0402_1005Metric, F.Cu at (124.6, 78.9)
- added U4: BQ25895RTW, Package_DFN_QFN:Texas_S-PWQFN-N24_EP2.7x2.7mm_ThermalVias, B.Cu at (112.1, 96.4)
- MK1: footprint penta:MIC_SPH0645LM4H-B -> Sensor_Audio:Knowles_SPH0645LM4H-6_3.5x2.65mm
- moved C2 5.50 mm to (105.5, 109.2), turned to 90 degrees
- moved U1 5.47 mm to (106.7, 106.1)
- moved C3 3.01 mm to (109.1, 105.0), turned to -90 degrees
- moved MK1 0.80 mm to (100.0, 88.2)
- moved R1 0.54 mm to (104.4, 109.2)
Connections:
- net Net-(MK1-BCLK) renamed /BCLK
- net Net-(MK1-WS) renamed /LRCLK
- U2 pad 30: /LED_DATA -> /I2S DATA
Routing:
- net +5V: track 302.3 -> 306.7 mm
- net +3V3: track 83.3 -> 81.4 mm
- net Net-(J1-CC1): track 4.67 -> 4.14 mm
- net GND: track 101.8 -> 102.3 mm, vias 153 -> 152
- net Net-(J1-SHIELD): track 16.7 -> 16.8 mm, vias 2 -> 0
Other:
- board size 37.4 x 37.4 mm -> 37.4 x 43.8 mm

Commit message: completely rework everything but the pixels; base it off seeeduino for ease/cost; add a usb port for chaining; add a microphone
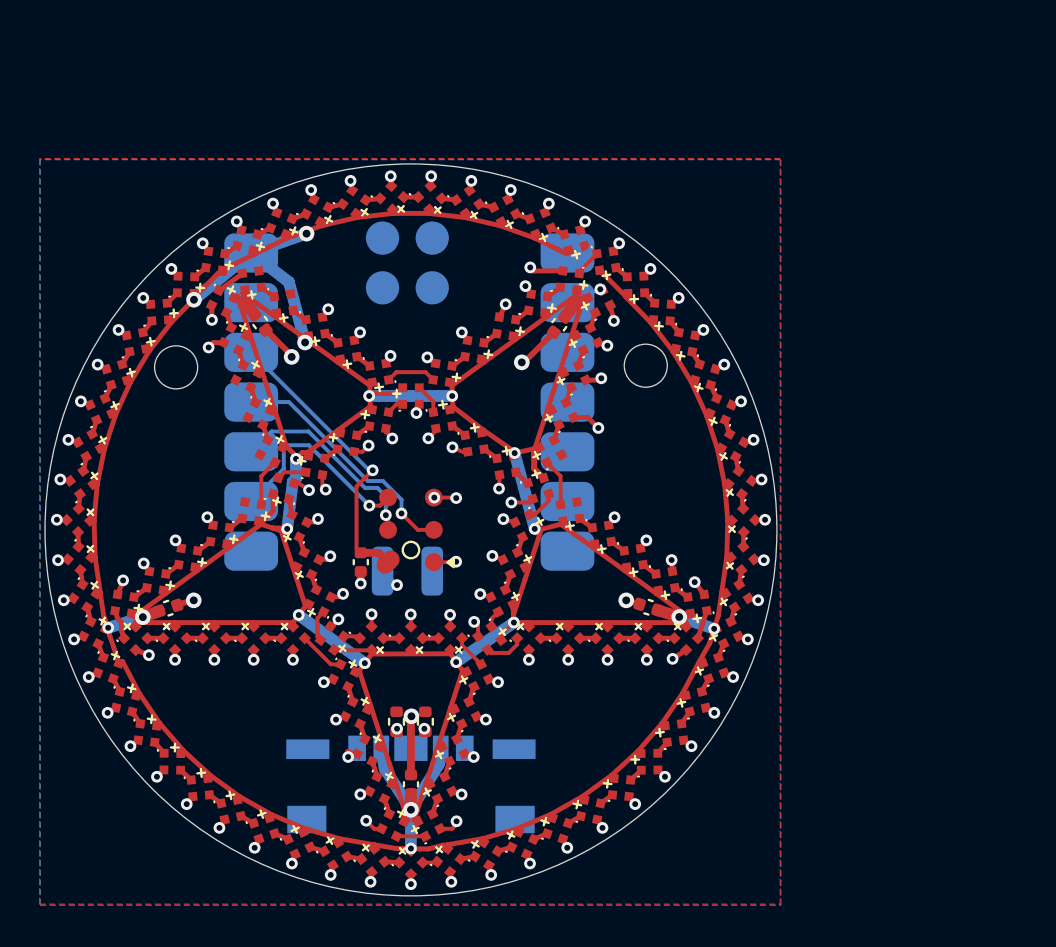
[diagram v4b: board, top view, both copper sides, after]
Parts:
- removed C10, C11, C12, C13, C14, C15, C17, C18, C19, C9: 100n, Capacitor_SMD:C_0402_1005Metric
- removed C16, C27, C29, C30, C8: 1u, Capacitor_SMD:C_0402_1005Metric
- removed C2, C3, C5: 1uF, Capacitor_SMD:C_0402_1005Metric
- removed C25: 10uF, Capacitor_SMD:C_0402_1005Metric
- removed C28: 47n, Capacitor_SMD:C_0402_1005Metric
- removed C4: 220pF, Capacitor_SMD:C_0402_1005Metric
- removed C6, C7: 27pF, Capacitor_SMD:C_0402_1005Metric
- removed J2: Conn_01x02, Connector_JST:JST_PH_S2B-PH-SM4-TB_1x02-1MP_P2.00mm_Horizontal
- removed MK1: SPH0645LM4H-B, Sensor_Audio:Knowles_SPH0645LM4H-6_3.5x2.65mm
- removed R3: 1M, Resistor_SMD:R_0402_1005Metric
- removed R4: 68, Resistor_SMD:R_0402_1005Metric
- removed R5: 10K, Resistor_SMD:R_0402_1005Metric
- removed R6: 1k, Resistor_SMD:R_0402_1005Metric
- removed R7, R8: 27, Resistor_SMD:R_0402_1005Metric
- removed TH1: Thermistor_NTC, Resistor_SMD:R_0402_1005Metric
- removed U2: RP2040, Package_DFN_QFN:QFN-56-1EP_7x7mm_P0.4mm_EP3.2x3.2mm
- removed U3: W25Q32JVSS, Package_SO:SOIC-8_5.23x5.23mm_P1.27mm
- removed U4: BQ25895RTW, Package_DFN_QFN:Texas_S-PWQFN-N24_EP2.7x2.7mm_ThermalVias
- removed Y1: 12000Hz, Crystal:Crystal_SMD_3215-2Pin_3.2x1.5mm
- added G***: LOGO, penta:sds5050, B.Cu at (100.0, 107.0)
- added MIC1: LMD4737T263-OY1, penta:LGA-6_L4.7-W3.8-P1.65_LMD4737T, F.Cu at (100.0, 100.0)
- C1: value 40u -> 100nF; footprint Capacitor_SMD:C_0201_0603Metric -> Capacitor_SMD:C_0402_1005Metric
- J1: value USB_C_Receptacle -> USB_C_Receptacle_PowerOnly_6P; footprint Connector_USB:USB_C_Receptacle_GCT_USB4110 -> penta:USB-C-SMD_TYPE-C-6P-QT073
- R1, R2: moved to F.Cu
- U1: value MIC5504-3.3YM5 -> XIAO-RP2040-SMD; footprint Package_TO_SOT_SMD:SOT-23-5 -> penta:XIAO-RP2040-SMD
- moved C1 25.8 mm to (97.4, 101.7), turned to -90 degrees
- moved U1 14.3 mm to (100.0, 93.5), turned to 180 degrees
- moved R2 4.21 mm to (99.3, 109.8), turned to 90 degrees
- moved R1 3.68 mm to (100.7, 109.8)
- moved J1 2.02 mm to (100.0, 113.0)
- turned D106 to -40.09 degrees
- turned D125 to -164.454 degrees
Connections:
- C1 pad 1: +5V -> +3V3
- R2 pad 1: GND -> Net-(J1-CC2)
- R2 pad 2: Net-(J1-CC2) -> GND
- U1 pad 1: +5V -> unconnected-(U1-GPIO26_A0_D0-Pad1)
- U1 pad 2: GND -> /LED_DATA
- U1 pad 3: +5V -> unconnected-(U1-GPIO28_A2_D2-Pad3)
- U1 pad 5: +3V3 -> unconnected-(U1-GPIO6_D4_SDA-Pad5)
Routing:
- net +3V3: track 81.4 -> 14.9 mm, vias 0 -> 1
- net GND: track 102.3 -> 82.3 mm, vias 152 -> 127
- net /QSPI_SS: track 17.0 -> 0.00 mm
- net Net-(J1-SHIELD): track 16.8 -> 0.00 mm
- net /QSPI1: track 16.6 -> 0.00 mm
- net +1V1: track 16.0 -> 0.00 mm, vias 3 -> 0
- net /QSPI3: track 14.8 -> 0.00 mm
- net /QSPI_SCK: track 13.7 -> 0.00 mm
- net /QSPI2: track 13.6 -> 0.00 mm
- net /LED_DATA: track 14.0 -> 2.18 mm
- net /I2S DATA: track 0.00 -> 10.4 mm, vias 0 -> 1
- net /QSPI0: track 10.1 -> 0.00 mm
- net +5V: track 306.7 -> 297.5 mm, vias 15 -> 19
- net Net-(U2-GPIO18): track 9.13 -> 0.00 mm
- net /USB D-: track 8.78 -> 0.00 mm, vias 2 -> 0
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- added copper zone on B.Cu, net GND
- added copper zone on F.Cu, net GND
- removed copper zone on In1.Cu, net GND
- removed copper zone on In2.Cu, net GND
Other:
- board size 37.4 x 43.8 mm -> 37.4 x 37.4 mm
- copper layers 4 -> 2
- board text added: "+5V"
- board text added: "3.3V"
- board text added: "BCLK"
- board text added: "GND"
- board text added: "I2SD"
- board text added: "LED"
- board text added: "LRCLK"
- board text added: "seeed xiao rp2040"
